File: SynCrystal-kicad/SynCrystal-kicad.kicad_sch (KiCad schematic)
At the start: 26 parts, among them CN1 PJ-342, J1 ICSP, J2 DIN-6 Male, SW1 Mode -, SW2 Mode +, SW3 Frame -, SW4 Frame +, SW5 Shaft_Pulse_Ratio, U2 ATmega328P-A

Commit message: Starting to assign part numbers
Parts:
- removed J2: DIN-6 Male, symbol Connector_Generic:Conn_01x07
- added C10, C12, C13, C14, C16, C2, C4, C8: 100n, Capacitor_SMD:C_0603_1608Metric, symbol Device:C_Small
- added C11, C9: 1u, Capacitor_SMD:C_0603_1608Metric, symbol Device:C_Small
- added C15: 330n, Capacitor_SMD:C_0603_1608Metric, symbol Device:C_Small
- added C17, C18, C19: 47u, Capacitor_SMD:C_1206_3216Metric, symbol Device:C_Small
- added C20, C6: 2u2, Capacitor_SMD:C_0603_1608Metric, symbol Device:C_Small
- added C21, C7: 10u, Capacitor_SMD:C_0805_2012Metric, symbol Device:C_Small
- added C3, C5: 22u, Capacitor_SMD:C_0805_2012Metric, symbol Device:C_Small
- added D1, D5, D6: LED, easyEDA:LED-SMD_MHS153IRCT, symbol easyEDA:XYC-IRA3212A25-X4_smaller
- added D2, D4, D7: B5819W SL, Diode_SMD:D_SOD-123, symbol Device:D_Schottky_Small
- added J4: Pause Button, symbol Connector_Generic:Conn_01x02
- added J5: to DIN-6 Male, symbol Connector_Generic:Conn_01x07
- added J6: DIN-6 male, symbol Connector:DIN-6
- added L1: 4.7uH, easyEDA:IND-SMD_L3.0-W3.0, symbol Device:L_Small
- added Q1, Q2, Q4: SS8050, Package_TO_SOT_SMD:SOT-23, symbol Transistor_BJT:BC847
- added Q3: AO3400A, Package_TO_SOT_SMD:SOT-23, symbol Transistor_FET:AO3400A
- added R10: 4k7, Resistor_SMD:R_0603_1608Metric, symbol Device:R_Small
- added R11, R5: 3k3, Resistor_SMD:R_0603_1608Metric, symbol Device:R_Small
- added R13, R15, R16, R27, R30, R6, R9: 10k, Resistor_SMD:R_0603_1608Metric, symbol Device:R_Small
- added R14: 2k7, Resistor_SMD:R_0603_1608Metric, symbol Device:R_Small
- added R17: 5R1, Resistor_SMD:R_0805_2012Metric, symbol Device:R_Small
- added R18, R19, R20, R29: 100k, Resistor_SMD:R_0603_1608Metric, symbol Device:R_Small
- added R21: 47, Resistor_SMD:R_0603_1608Metric, symbol Device:R_Small
- added R22: 10, Resistor_SMD:R_0603_1608Metric, symbol Device:R_Small
- added R23: 22k, Resistor_SMD:R_0603_1608Metric, symbol Device:R_Small
- added R24, R31: 100, Resistor_SMD:R_0603_1608Metric, symbol Device:R_Small
- added R28: 470, Resistor_SMD:R_0603_1608Metric, symbol Device:R_Small
- added R35, R4: 220k, Resistor_SMD:R_0603_1608Metric, symbol Device:R_Small
- added R7: 47k, Resistor_SMD:R_0603_1608Metric, symbol Device:R_Small
- added R8: 470k, Resistor_SMD:R_0603_1608Metric, symbol Device:R_Small
- added RV1: 10k, easyEDA:RES-SMD_RK10J11R0A0H, symbol Device:R_Potentiometer_Small
- added RV2: 300, easyEDA:RES-SMD_RK10J11R0A0H, symbol Device:R_Potentiometer_Small
- added SW6: Guide/Follow, symbol Switch:SW_SPDT
- added TP10: Imp IN, TestPoint:TestPoint_Pad_D1.0mm, symbol Peacemans Teile:TestPoint_named
- added TP11: Imp cln, TestPoint:TestPoint_Pad_D1.0mm, symbol Peacemans Teile:TestPoint_named
- added TP12: DAC, TestPoint:TestPoint_Pad_D1.0mm, symbol Peacemans Teile:TestPoint_named
- added TP7: 5V, TestPoint:TestPoint_Pad_D1.0mm, symbol Peacemans Teile:TestPoint_named
- added TP8: 3V3, TestPoint:TestPoint_Pad_D1.0mm, symbol Peacemans Teile:TestPoint_named
- added TP9: 678, TestPoint:TestPoint_Pad_D1.0mm, symbol Peacemans Teile:TestPoint_named
- added U1: 74HCT14, Package_SO:TSSOP-14_4.4x5mm_P0.65mm, symbol Peacemans Teile:74HCT14
- added U10: MCP4725, Package_TO_SOT_SMD:SOT-23-6, symbol Analog_DAC:MCP4725xxx-xCH
- added U3: AP2210N-3.3TRG1, Package_TO_SOT_SMD:SOT-23-3, symbol easyEDA:AP2210N-3.3TRG1
- added U4: ECS-TXO-3225MV-160-TR, Crystal:Crystal_SMD_3225-4Pin_3.2x2.5mm, symbol easyEDA:ECS-TXO-3225MV-160-TR
- added U5: AP63205WU, Package_TO_SOT_SMD:TSOT-23-6, symbol Regulator_Switching:AP63205WU
- added U6, U8: LMC6482, Package_SO:SOIC-8_3.9x4.9mm_P1.27mm, symbol Amplifier_Operational:LMC6482
- added U7: G3VM-61VY3(TR), easyeda2kicad:SOP-4_L3.9-W4.4-P2.54-LS7.0-BR, symbol easyEDA:G3VM-61VY3(TR)_smaller
- added U9: TSOP34838, OptoDevice:Vishay_MOLD-3Pin, symbol Interface_Optical:TSOP348xx
- C1: LCSC (none) -> C14663
- CN1: LCSC (none) -> C668606; LCSC Part C668606 -> (none)
- R1, R2: LCSC (none) -> C4190
- R12, R25, R26: LCSC (none) -> C25803
- R3: LCSC (none) -> C25804
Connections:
- net +5V: now also C10.1, C11.2, C12.2, C16.1, C17.1, C18.1, C19.1, C3.1, C5.1, C9.1, D2.1 (K), L1.2, Q4.3 (C), R17.1, R31.1, R4.1, R5.2, R6.2, R7.1, TP7.1, U1.14 (VCC), U10.3 (VDD), U3.3 (VIN), U5.1 (FB), U6.8 (V+)
- net DAC_EN: now also J5.5 (Pin_5)
- net D_POT: now also U9.1 (OUT)
- net Ext_Imp_LED: now also Q2.3 (C)
- net GND: now also C10.2, C11.1, C12.1, C15.1, C16.2, C17.2, C18.2, C19.2, C20.2, C21.2, C3.2, C4.2, C5.2, C6.2, C7.2, C8.2, C9.2, D4.2 (A), J5.7 (Pin_7), Q1.2 (E), Q2.2 (E), Q3.2 (S), R10.1, R18.1, R19.1, R20.2, R21.2, R23.2, R29.2, R30.2, R35.1, U1.7 (GND), U10.2 (VSS), U10.6 (A0), U3.1 (GND), U4.2 (GND), U5.4 (GND), U6.4 (V-), U7.2, U9.2 (GND)
- net INT0: now also U1.10
- net INT1: now also C14.2, TP11.1, U1.8
- net IRSEND: now also R22.1, R23.1, R24.2
- net M-Pin: now also J5.2 (Pin_2), R15.1
- net MISO: now also SW6.2 (B)
- net Pin_678: now also J5.3 (Pin_3), R14.1, TP9.1, U6.1
- net Proj_Vcc: now also C7.1, J5.1 (Pin_1), U5.2 (EN), U5.3 (IN)
- net SCL: now also U10.5 (SCL)
- net SDA: now also U10.4 (SDA)
- net Stop_EN: now also J5.4 (Pin_4)
- net uC-Clock: now also U1.6
- net ESS in/Impulse_IN: no longer names the net of CN1.5
- net ESS in/Impulse_IN: now also R13.2, TP10.1
- new net: R11.1, U1.12
- new net: Q1.3 (C), R5.1, R8.2, U1.13
- new net: R21.1, RV1.1
- new net: RV1.2, U8.6 (-)
- new net: R16.2, RV1.3, U8.7
- new net: U1.3, U4.3 (Output)
- new net: U1.4, U1.5
- new net: D6.1 (A), R17.2
- new net: C20.1, D7.1 (K), R27.1, R29.1
- new net: D7.2 (A), R24.1
- new net: C13.1, D2.2 (A), D4.1 (K), R13.1, R18.2
- new net: C14.1, Q2.1 (B), R20.1
- new net: C15.2, R16.1, U1.1
- new net: C8.1, R11.2, U1.11
- new net: R4.2, SW6.1 (A)
- new net: R14.2, RV2.3
- new net: C13.2, R19.2, U8.5 (+)
- new net: R35.2, SW6.3 (C)
- new net: U1.2, U1.9
- new net: Q4.2 (E), R28.1, R30.1
- new net: C21.1, R31.2, U9.3 (Vs)
- new net: Q1.1 (B), R15.2, R7.2, R8.1
- new net: R9.1, RV2.2, U6.2 (-)
- new net: R9.2, TP12.1, U10.1 (VOUT)
- new net: Q3.1 (G), R22.2
- new net: D1.2 (K), Q3.3 (D)
- new net: R10.2, R6.1, U6.3 (+)
- new net: D5.1 (A), D6.2 (K)
- new net: R28.2, U7.1
- new net: C2.1, L1.1, U5.5 (SW)
- new net: C2.2, U5.6 (BST)
- new net: Q4.1 (B), R27.2
- new net: J4.2 (Pin_2), U7.3
- new net: J4.1 (Pin_1), U7.4
- new net: D1.1 (A), D5.2 (K)
- new net +3.3V: C4.1, C6.1, TP8.1, U3.2 (VOUT), U4.4 (VDD)
- no-connect marks 2 -> 3
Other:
- removed sheet DAC
- removed sheet ESS in
- removed sheet Frontpanel UI
- removed sheet GuideStart
- removed sheet PSU
- removed sheet Projector Impulse Cleaning
- removed sheet TCXO
- note added: "0.55-1.95V"
- note added: "Buttons"
- note added: "Cable"
- note added: "DAC"
- note added: "Display"
- note added: "ESS-in"
- note added: "Für 0,5-1,5V: R9 12k, R14 2k2 Für 0.6-1.9V: R9 10k, R14 2k8"
- note added: "IR I/O"
- note added: "Other imagineable pulse sources: - S/PDIF / TOSLINK Clock - Video FBAS - Pulse Head - Start Beep"
- note added: "PSU"
- note added: "Pulse Cleaner"
- note added: "TCXO"
- note added: "To Do: - Effektiven DAC-OpAmps Range an 678 messen - Stop-Spannung messen - Monoflop auf Relaisplatine testen - Schottky an Lampe testen - INT1 wegsparen? (2 Schottkys) - Startpiepser statt ESS Impulen erkennen Consider: - 5V vom Projektor holen statt 15V doppelt wandeln - DAC-Opamp aufs Projektor-Board? - Dann aber auch Projektor-Erkennung über Spannungsteiler an DAC_EN, der dann an A0 muss"
- note added: "Works with 1000 Hz Bursts as well as square waves from 3-99% duty cylce"
- note added: "to Frontpanel"
- note added: "µC"
- note removed: "Other imagineable pulse sources: - S/PDIF / TOSLINK Clock - Video FBAS - Pulse Head"
- note removed: "To Do: - Frontpanel separieren - Guide/Follow Selector - INT1 wegsparen? (2 Schottkys) - Startpiepser statt ESS Impulen erkennen"
- company: (none) -> filmkorn.org
- title: (none) -> SynCrystal Controller
- moved on the sheet: C1, CN1, D3, J1, J3, JP1, JP2, R1, R12, R2, R25, R26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

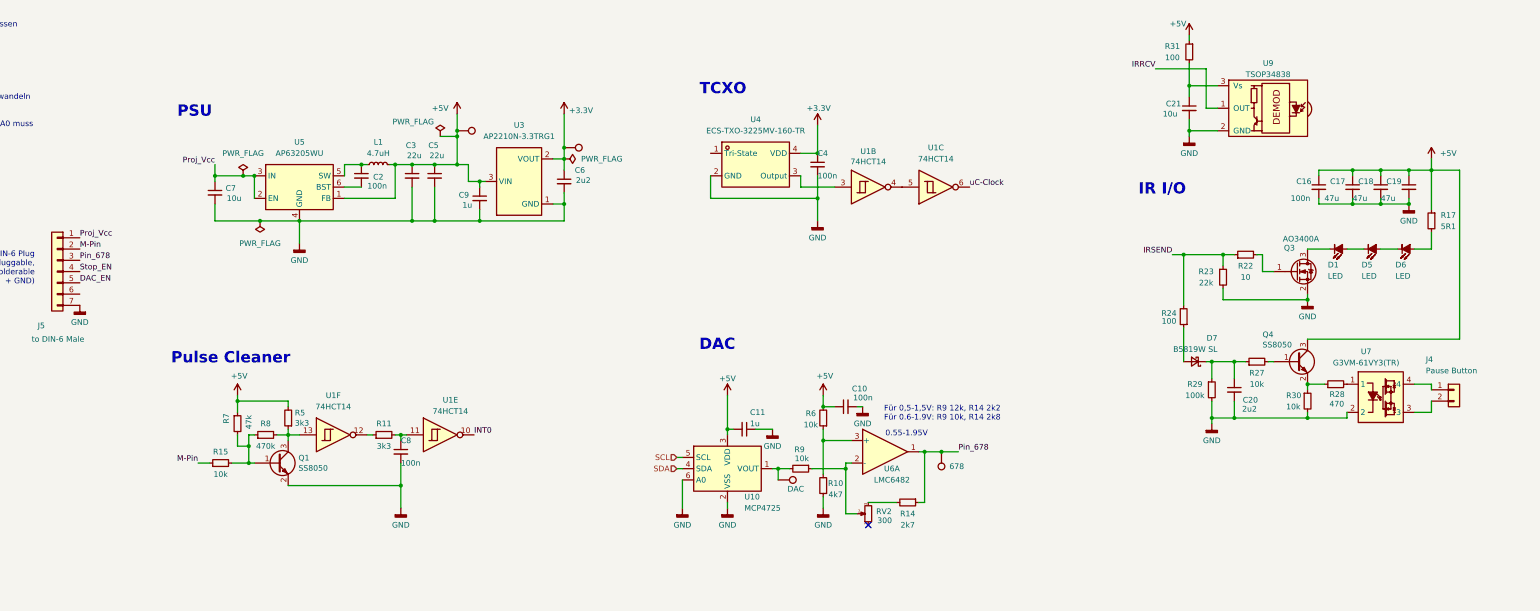
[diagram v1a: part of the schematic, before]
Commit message: Moved the OpAmp to the Projector Board. This Layout is DRC 0, but not optimal
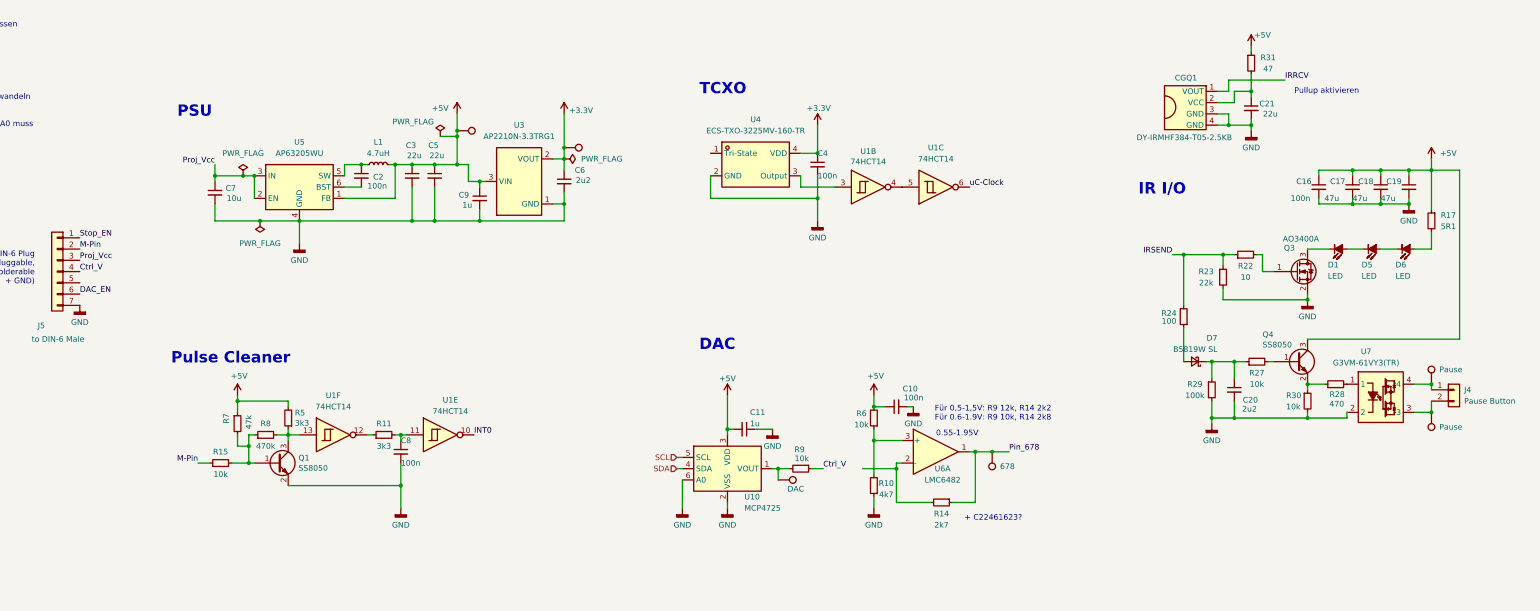
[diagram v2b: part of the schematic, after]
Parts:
- removed RV2: 300, easyEDA:RES-SMD_RK10J11R0A0H, symbol Device:R_Potentiometer_Small
- removed U9: TSOP34838, OptoDevice:Vishay_MOLD-3Pin, symbol Interface_Optical:TSOP348xx
- added CGQ1: DY-IRMHF384-T05-2.5KB, easyEDA:OPTO-SMD_4P-L3.9-W3.4_IRM-H432M3-R8, symbol easyEDA:DY-IRMHF384-T05-2.5KB
- added TP13, TP14: Pause, TestPoint:TestPoint_Pad_D1.0mm, symbol Peacemans Teile:TestPoint_named
- C21: value 10u -> 22u; LCSC C15850 -> C45783
- D1, D5, D6: LCSC Part C6081333 -> (none)
- J4: footprint (none) -> easyEDA:CONN-TH_DB125-2.54-2P-GN; LCSC (none) -> C918120
- J5: footprint (none) -> easyEDA:CONN-TH_S7B-XH-A-LF-SN; LCSC (none) -> C157916
- R31: value 100 -> 47; LCSC C22775 -> C23182
- SW1, SW2, SW3, SW4: footprint Button_Switch_SMD:SW_SPST_PTS647_Sx50 -> easyEDA:SW-SMD_4P-L6.0-W6.0-P4.50-LS9.0_TS-1002S-08026C; LCSC (none) -> C455116
- SW5: footprint (none) -> easyEDA:SW-SMD_MSK13C02-SZ; LCSC (none) -> C2681567
- SW6: footprint (none) -> easyEDA:SW-TH_MSK12C02-HB-1; LCSC (none) -> C431541
- U10: LCSC (none) -> C144198
- U2: LCSC (none) -> C14877
- U3: LCSC (none) -> C155508
- U5: LCSC (none) -> C2071056
- U6, U8: LCSC (none) -> C12620
- U7: footprint easyeda2kicad:SOP-4_L3.9-W4.4-P2.54-LS7.0-BR -> easyEDA:SOP-4_L3.9-W4.4-P2.54-LS7.0-BR; LCSC (none) -> C2152318
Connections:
- net DAC_EN: now also J5.6 (Pin_6); no longer J5.5 (Pin_5)
- net D_POT: now also CGQ1.1 (VOUT)
- net GND: now also CGQ1.3 (GND), CGQ1.4 (GND)
- net Pin_678: no longer J5.3 (Pin_3)
- net Proj_Vcc: now also J5.3 (Pin_3); no longer J5.1 (Pin_1)
- net Stop_EN: now also J5.1 (Pin_1); no longer J5.4 (Pin_4)
- net at R14.2: now also U6.2 (-)
- net at C21.1, R31.2: now also CGQ1.2 (VCC)
- net Ctrl_V: now reaches R9.1
- net Ctrl_V: now also J5.4 (Pin_4); no longer U6.2 (-)
- net at J4.2 (Pin_2), U7.3: now also TP13.1
- net at J4.1 (Pin_1), U7.4: now also TP14.1
- no-connect marks 3 -> 2
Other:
- note added: "+ C22461623?"
- note added: "Pullup aktivieren"
- moved on the sheet: C10, C21, R10, R14, R31, R6, U6A

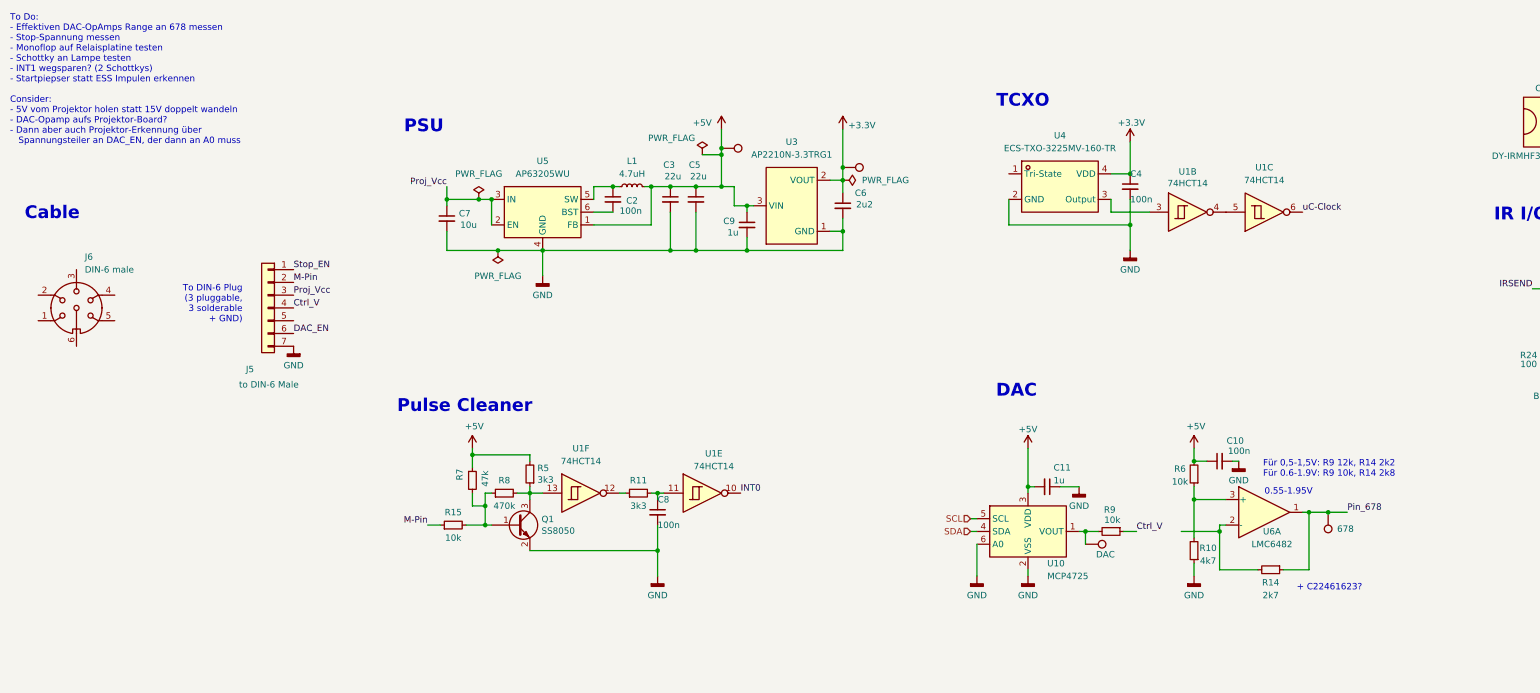
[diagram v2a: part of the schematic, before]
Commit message: moving the 10k OpAmp Input R to the Projector board
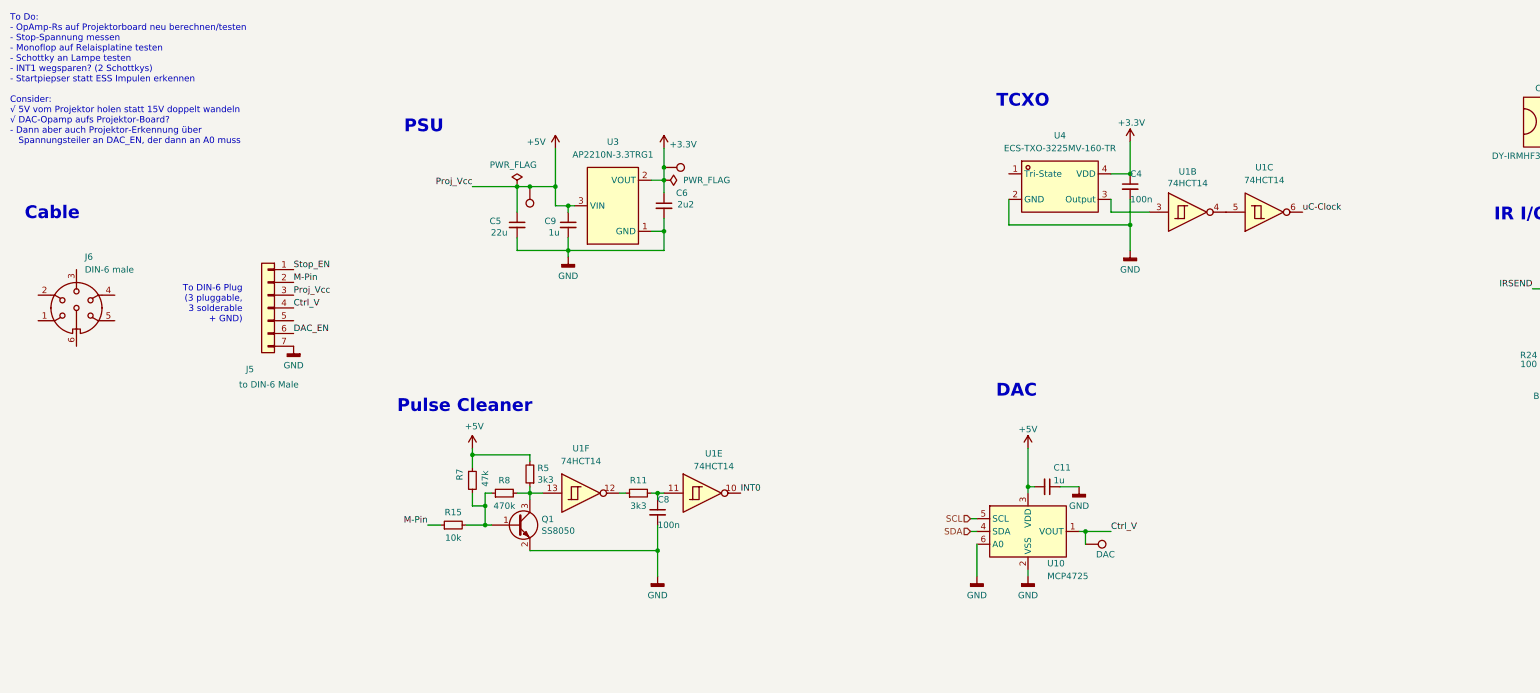
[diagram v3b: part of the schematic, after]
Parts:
- removed C10, C2: 100n, Capacitor_SMD:C_0603_1608Metric, symbol Device:C_Small
- removed C3: 22u, Capacitor_SMD:C_0805_2012Metric, symbol Device:C_Small
- removed C7: 10u, Capacitor_SMD:C_0805_2012Metric, symbol Device:C_Small
- removed L1: 4.7uH, easyEDA:IND-SMD_L3.0-W3.0, symbol Device:L_Small
- removed R10: 4k7, Resistor_SMD:R_0603_1608Metric, symbol Device:R_Small
- removed R14: 2k7, Resistor_SMD:R_0603_1608Metric, symbol Device:R_Small
- removed R6, R9: 10k, Resistor_SMD:R_0603_1608Metric, symbol Device:R_Small
- removed TP9: 678, TestPoint:TestPoint_Pad_D1.0mm, symbol Peacemans Teile:TestPoint_named
- removed U5: AP63205WU, Package_TO_SOT_SMD:TSOT-23-6, symbol Regulator_Switching:AP63205WU
- removed unit 1 of U6
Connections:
- net Proj_Vcc is gone; now on net +5V: J5.3 (Pin_3)
- net Ctrl_V: now also TP12.1, U10.1 (VOUT)
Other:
- note added: "To Do: - OpAmp-Rs auf Projektorboard neu berechnen/testen - Stop-Spannung messen - Monoflop auf Relaisplatine testen - Schottky an Lampe testen - INT1 wegsparen? (2 Schottkys) - Startpiepser statt ESS Impulen erkennen Consider: √ 5V vom Projektor holen statt 15V doppelt wandeln √ DAC-Opamp aufs Projektor-Board? - Dann aber auch Projektor-Erkennung über Spannungsteiler an DAC_EN, der dann an A0 mu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"
- note removed: "+ C22461623?"
- note removed: "0.55-1.95V"
- note removed: "Für 0,5-1,5V: R9 12k, R14 2k2 Für 0.6-1.9V: R9 10k, R14 2k8"
- note removed: "To Do: - Effektiven DAC-OpAmps Range an 678 messen - Stop-Spannung messen - Monoflop auf Relaisplatine testen - Schottky an Lampe testen - INT1 wegsparen? (2 Schottkys) - Startpiepser statt ESS Impulen erkennen Consider: - 5V vom Projektor holen statt 15V doppelt wandeln - DAC-Opamp aufs Projektor-Board? - Dann aber auch Projektor-Erkennung über Spannungsteiler an DAC_EN, der dann an A0 muss"
- moved on the sheet: C5, C6, C9, U3

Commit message: Adding the VOltage Divider to Projector Board to allow Projector Detection. Also, fixing various footprints on the controller. ERC now failing.
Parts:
- removed R25, R26: 100k, Resistor_SMD:R_0603_1608Metric, symbol Device:R_Small
- removed SW5: Shaft_Pulse_Ratio, easyEDA:SW-SMD_MSK13C02-SZ, symbol Switch:SW_SP3T
- removed U6, U8: LMC6482, Package_SO:SOIC-8_3.9x4.9mm_P1.27mm, symbol Amplifier_Operational:LMC6482
- added C2: 100n, Capacitor_SMD:C_0603_1608Metric, symbol Device:C_Small
- added H1, H2: MountingHole, MountingHole:MountingHole_4.3mm_M4_ISO14580, symbol Mechanical:MountingHole
- added R6: 220k, Resistor_SMD:R_0603_1608Metric, symbol Device:R_Small
- added U5: LMC6482, Package_SO:SOIC-8_3.9x4.9mm_P1.27mm, symbol Amplifier_Operational:LMC6482
- D1, D5, D6: footprint easyEDA:LED-SMD_MHS153IRCT -> easyEDA:LED-SMD_XYC-IRA4335A65-X4; symbol easyEDA:XYC-IRA3212A25-X4_smaller -> easyEDA:XYC-IRA4335A65-X4; LCSC C6081333 -> C2920776; LCSC Part (none) -> C2920776
- J4: footprint easyEDA:CONN-TH_DB125-2.54-2P-GN -> easyEDA:CONN-TH_2P-P2.54_MX128-2.54-GN01-02P-CU-Y-A
- RV1: footprint easyEDA:RES-SMD_RK10J11R0A0H -> easyEDA:RES-SMD_RK10J11R0A0H_fixed
- SW1, SW2, SW3, SW4: symbol Switch:SW_Push -> easyEDA:SW-C455116-nicer; LCSC Part (none) -> C93156
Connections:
- net +5V: now also U5.8 (V+)
- net Frame+: now also SW4.1
- net Frame-: now also SW3.1
- net GND: now also SW1.3, SW1.4, SW2.3, SW2.4, SW3.3, SW3.4, SW4.3, SW4.4, C2.2, R6.2, U5.3 (+), U5.4 (V-); no longer SW1.1, SW2.1, SW3.1, SW4.1
- net Mode+: now also SW2.1
- net Mode-: now also SW1.1
- net at RV1.2: now also U5.6 (-)
- net at R16.2, RV1.3: now also U5.7
- net Proj_ID: now reaches U2.23 (PC0)
- net Proj_ID: now also J5.5 (Pin_5), C2.1, R6.1
- net at R17.2: now also D1.2 (A); no longer D6.1 (A)
- net at C13.2, R19.2: now also U5.5 (+)
- net at Q3.3 (D): now also D6.1 (K); no longer D1.2 (K)
- new net: U5.1, U5.2 (-)
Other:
- note added: "To Do: - OpAmp-Rs auf Projektorboard neu berechnen/testen - Stop-Spannung messen - Monoflop auf Relaisplatine testen - Schottky an Lampe testen - INT1 wegsparen? (2 Schottkys) - Startpiepser statt ESS Impulen erkennen Consider: - Projektor-Erkennung (für Imp-Ratio) über Spannungsteiler an DAC_EN, der dann an A0 muss"
- note removed: "To Do: - OpAmp-Rs auf Projektorboard neu berechnen/testen - Stop-Spannung messen - Monoflop auf Relaisplatine testen - Schottky an Lampe testen - INT1 wegsparen? (2 Schottkys) - Startpiepser statt ESS Impulen erkennen Consider: √ 5V vom Projektor holen statt 15V doppelt wandeln √ DAC-Opamp aufs Projektor-Board? - Dann aber auch Projektor-Erkennung über Spannungsteiler an DAC_EN, der dann an A0 mu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"
- moved on the sheet: SW1, SW2, SW3, SW4
